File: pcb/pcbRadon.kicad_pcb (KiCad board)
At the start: 2 copper layers, 57.4 x 31.5 mm, 13 parts, among them J1 Conn_01x02, J2 Jack-DC, J3 Conn_01x06, J4 RTC, K1 SANYOU_SRD_Form_C, Q1 TIP120, U1 Wemos, U2 Step-down

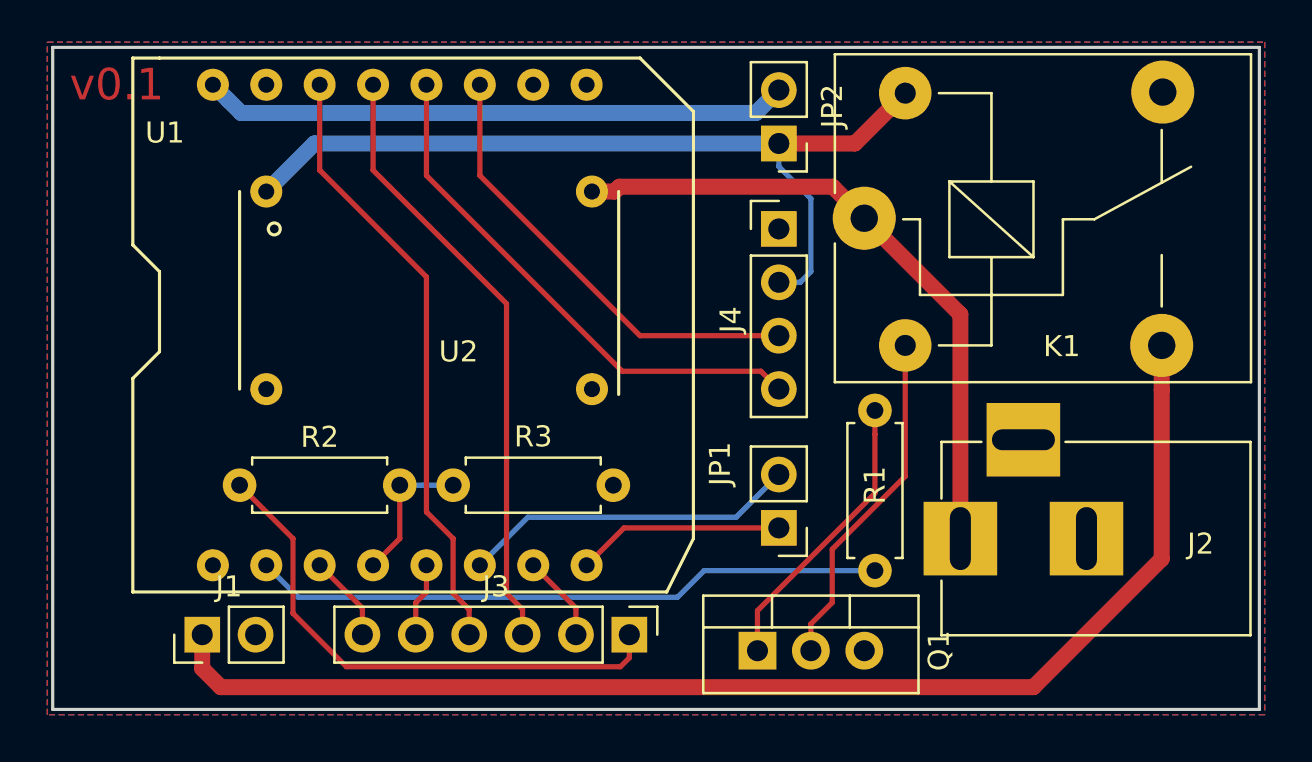
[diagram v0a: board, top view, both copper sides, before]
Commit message: Fixed connection to relay (normaly close) and add silkscreen texts
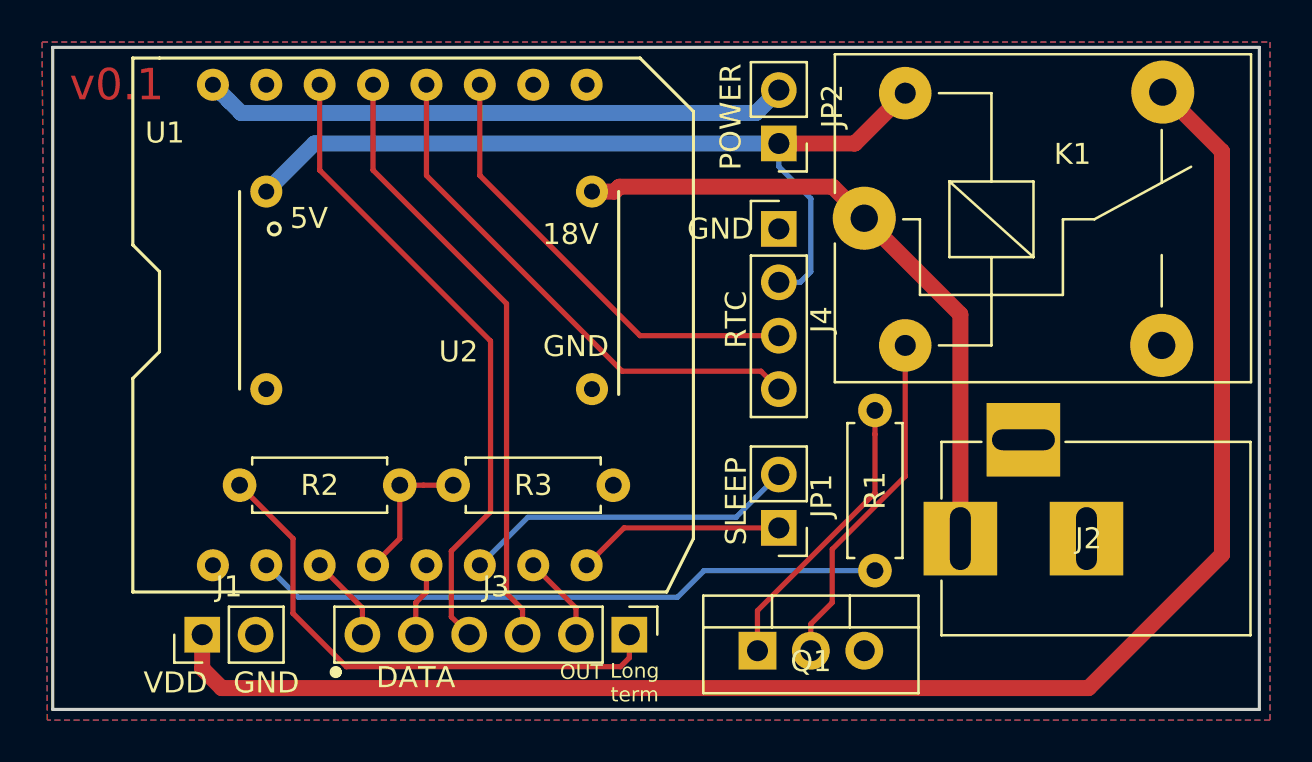
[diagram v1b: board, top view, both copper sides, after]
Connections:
- K1 pad 3: Net-(J1-Pad1) -> Net-(K1-Pad3)
- K1 pad 4: Net-(K1-Pad4) -> Net-(J1-Pad1)
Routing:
- net Net-(J1-Pad1): track 60.3 -> 76.3 mm
- net Net-(J3-Pad4): track 29.1 -> 30.7 mm
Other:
- board text added: "18V"
- board text added: "5V"
- board text added: "DATA"
- board text added: "GND"
- board text added: "Long term"
- board text added: "OUT"
- board text added: "POWER"
- board text added: "RTC"
- board text added: "SLEEP"
- board text added: "VDD"
